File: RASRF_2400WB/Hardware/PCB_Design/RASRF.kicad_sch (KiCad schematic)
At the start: 76 parts, among them J3 60312202111527, J4 Conn_01x04_Pin, U1 LD1117S18TR_SOT223, U2 STM32C031G6Ux, U3 SN74AXC4T774RSVR, Y1 7L-40.000MBS-T, Y2 ABM10-166-12.000MHZ-T3

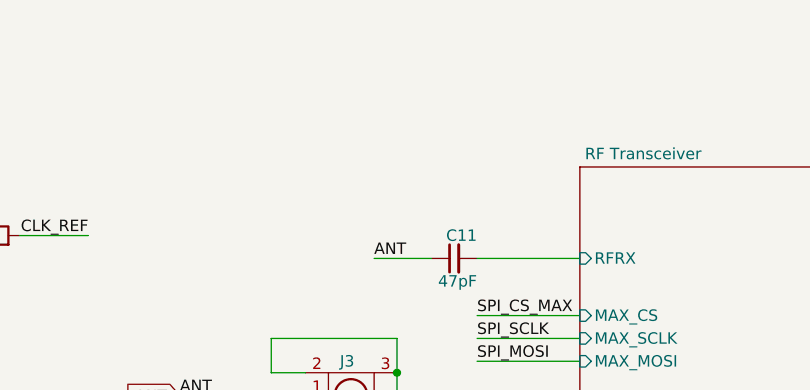
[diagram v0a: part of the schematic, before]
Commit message: Corrected the RASRF_2400WB PCB design files. They where not the latest from Rev. A. sent to manufacturer.
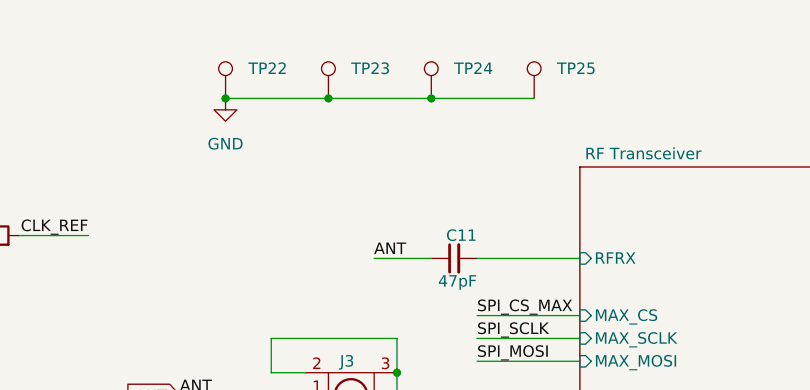
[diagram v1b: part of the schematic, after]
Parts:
- added TP22, TP23, TP24, TP25: TestPoint, TestPoint:TestPoint_Pad_D1.5mm, symbol Connector:TestPoint
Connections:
- net GND: now also TP22.1, TP23.1, TP24.1, TP25.1
